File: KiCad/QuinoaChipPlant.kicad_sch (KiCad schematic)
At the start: 25 parts, among them J1 POWER_SW, J2 POWER, J3 MOTOR, J4 SPEAKER, J5 NeoPixel, J6 Conn_01x04_Male, J7 COMMUNUCATE, J8 Conn_01x04_Male, J9 Conn_01x01_Female, Q1 Q_NMOS_GSD, U1 SparkFun_TB6612FNG_MOTOR_DRIV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, U2 SparkFun_Pro_Micro_328U4, U3 MIC5205-3.3YM5, U4 TSPCBA-01-B2_nRF52810_module

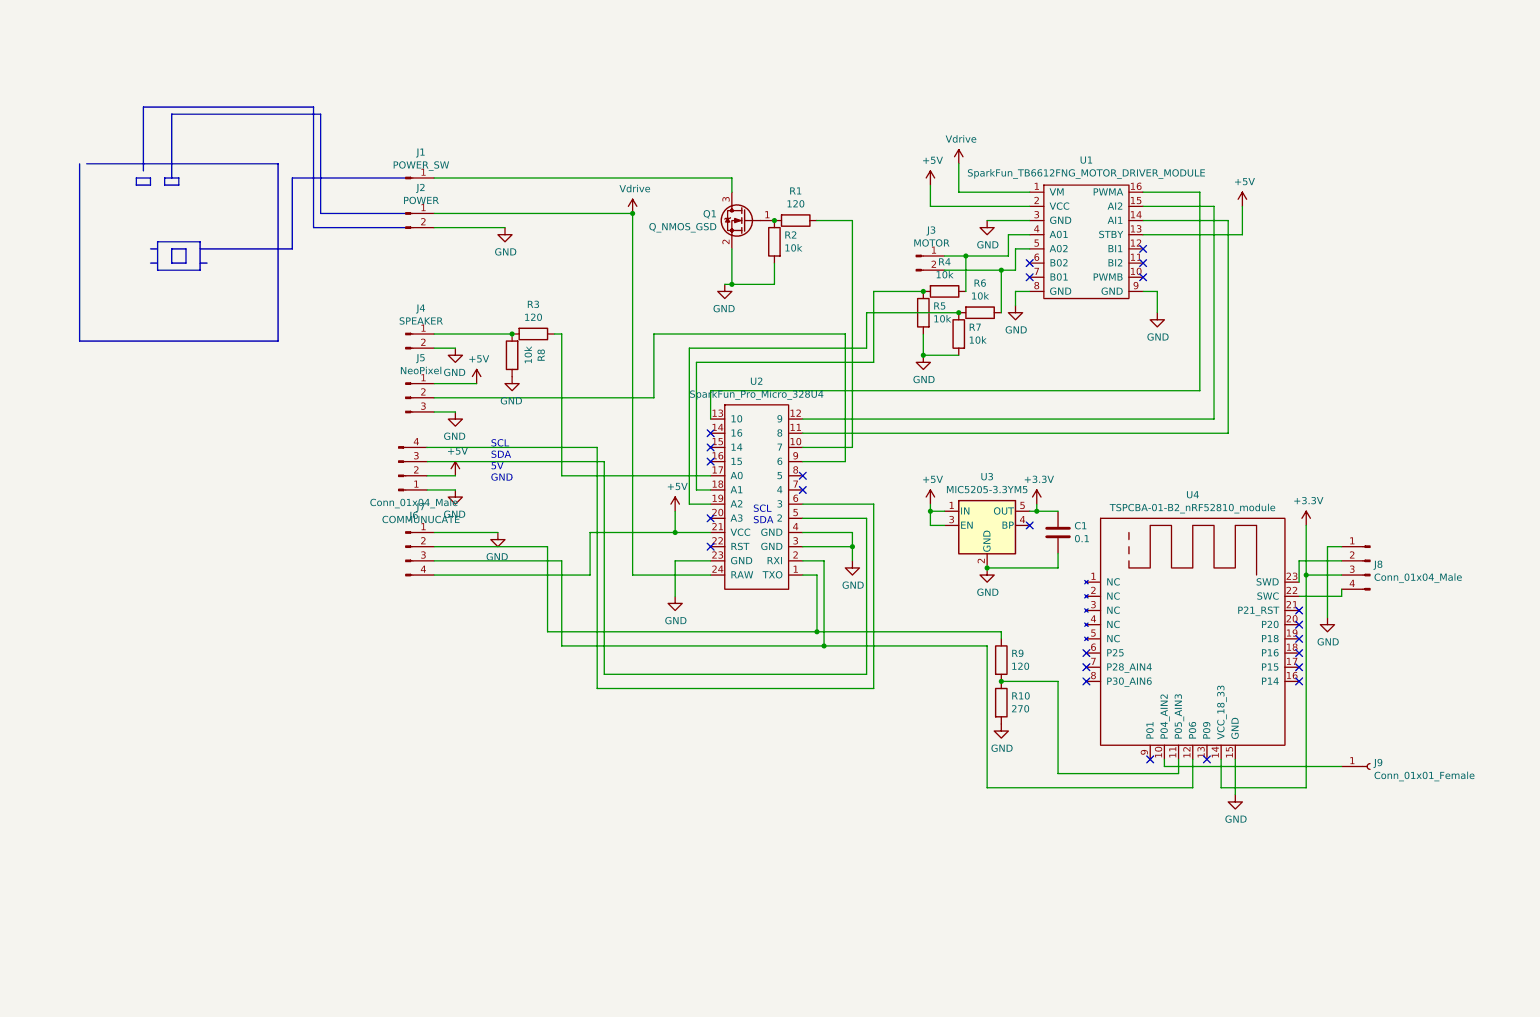
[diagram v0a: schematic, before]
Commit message: make pump, bulb , sensor PCB.
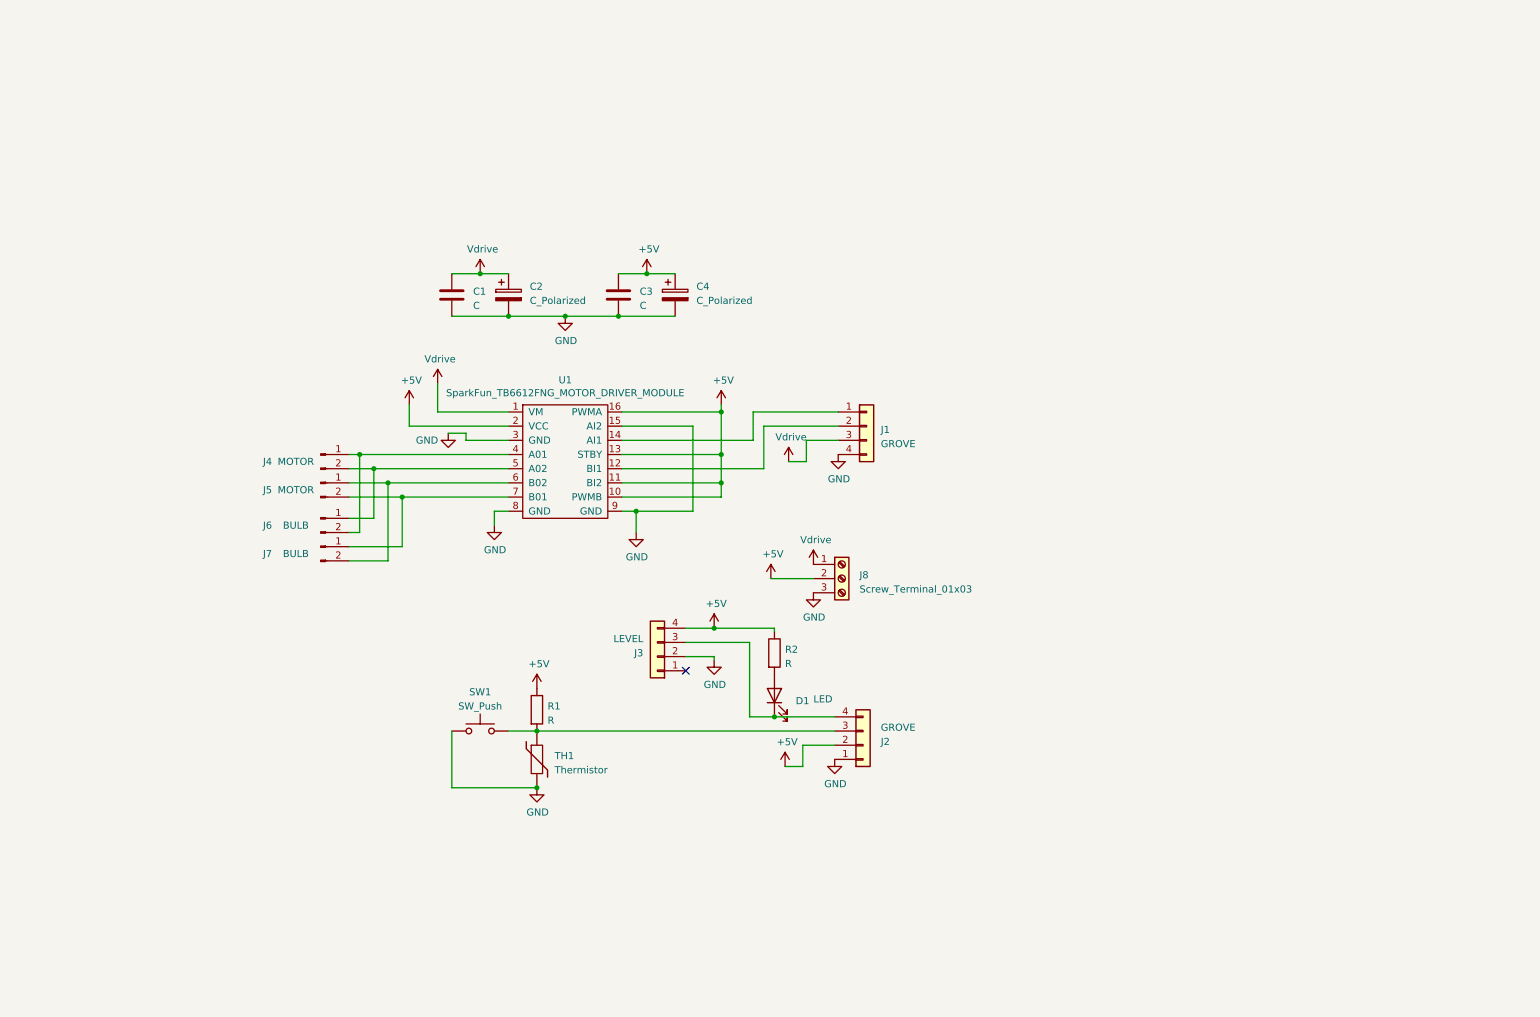
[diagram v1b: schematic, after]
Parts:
- removed J1: POWER_SW, Connector_PinHeader_2.54mm:PinHeader_1x01_P2.54mm_Vertical, symbol Connector:Conn_01x01_Male
- removed J2: POWER, Connector_PinHeader_2.54mm:PinHeader_1x02_P2.54mm_Vertical, symbol Connector:Conn_01x02_Male
- removed J4: SPEAKER, Connector_PinHeader_2.54mm:PinHeader_1x02_P2.54mm_Vertical, symbol Connector:Conn_01x02_Male
- removed J5: NeoPixel, Connector_PinHeader_2.54mm:PinHeader_1x03_P2.54mm_Vertical, symbol Connector:Conn_01x03_Male
- removed J6: Conn_01x04_Male, Connector_JST:JST_PH_B4B-PH-K_1x04_P2.00mm_Vertical, symbol Connector:Conn_01x04_Male
- removed J7: COMMUNUCATE, Connector_PinHeader_2.54mm:PinHeader_1x04_P2.54mm_Vertical, symbol Connector:Conn_01x04_Male
- removed J8: Conn_01x04_Male, Connector_PinHeader_2.54mm:PinHeader_1x04_P2.54mm_Vertical, symbol Connector:Conn_01x04_Male
- removed J9: Conn_01x01_Female, Connector_PinHeader_2.54mm:PinHeader_1x01_P2.54mm_Vertical, symbol Connector:Conn_01x01_Female
- removed Q1: Q_NMOS_GSD, Package_TO_SOT_SMD:SOT-23, symbol Device:Q_NMOS_GSD
- removed R10: 270, Resistor_SMD:R_0603_1608Metric, symbol Device:R
- removed R3, R9: 120, Resistor_SMD:R_0603_1608Metric, symbol Device:R
- removed R4, R5, R6, R7, R8: 10k, Resistor_SMD:R_0603_1608Metric, symbol Device:R
- removed U2: SparkFun_Pro_Micro_328U4, library:SparkFun_Pro_Micro_32U4, symbol QuinoaChipPlant-rescue:SparkFun_Pro_Micro_328U4-nanbuwks
- removed U3: MIC5205-3.3YM5, Package_TO_SOT_SMD:SOT-23-5, symbol Regulator_Linear:MIC5205-3.3YM5
- removed U4: TSPCBA-01-B2_nRF52810_module, library:TSPCBA-01-B2_nRF52810_module, symbol QuinoaChipPlant-rescue:TSPCBA-01-B2_nRF52810_module-nanbuwks
- added C2, C4: C_Polarized, Capacitor_SMD:C_1206_3216Metric_Pad1.33x1.80mm_HandSolder, symbol Device:C_Polarized
- added C3: C, Capacitor_SMD:C_1206_3216Metric_Pad1.33x1.80mm_HandSolder, symbol Device:C
- added D1: LED, symbol Device:LED
- added J1, J2: GROVE, Connector_JST:JST_PH_B4B-PH-K_1x04_P2.00mm_Vertical, symbol Connector_Generic:Conn_01x04
- added J3: LEVEL, Connector_JST:JST_XH_B4B-XH-AM_1x04_P2.50mm_Vertical, symbol Connector_Generic:Conn_01x04
- added J5: MOTOR, TerminalBlock_Phoenix:TerminalBlock_Phoenix_MPT-0,5-2-2.54_1x02_P2.54mm_Horizontal, symbol Connector:Conn_01x02_Male
- added J6, J7: BULB, Connector_JST:JST_XH_B2B-XH-AM_1x02_P2.50mm_Vertical, symbol Connector:Conn_01x02_Male
- added J8: Screw_Terminal_01x03, TerminalBlock_Philmore:TerminalBlock_Philmore_TB133_1x03_P5.00mm_Horizontal, symbol Connector:Screw_Terminal_01x03
- added SW1: SW_Push, Button_Switch_THT:SW_PUSH_6mm, symbol Switch:SW_Push
- added TH1: Thermistor, TerminalBlock:TerminalBlock_Altech_AK300-2_P5.00mm, symbol Device:Thermistor
- C1: value 0.1 -> C; footprint Capacitor_SMD:C_0603_1608Metric -> Capacitor_SMD:C_1206_3216Metric_Pad1.33x1.80mm_HandSolder
- J4: renamed from J3; footprint Connector_PinHeader_2.54mm:PinHeader_1x02_P2.54mm_Vertical -> TerminalBlock_Phoenix:TerminalBlock_Phoenix_MPT-0,5-2-2.54_1x02_P2.54mm_Horizontal
- R1: value 120 -> R; footprint Resistor_SMD:R_0603_1608Metric -> Resistor_SMD:R_1206_3216Metric_Pad1.30x1.75mm_HandSolder
- R2: value 10k -> R; footprint Resistor_SMD:R_0603_1608Metric -> Resistor_SMD:R_1206_3216Metric_Pad1.30x1.75mm_HandSolder
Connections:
- net +3V3 is gone; now on net Vdrive: C1.1
- net +5V: now also R1.1, R2.1, U1.10 (PWMB), U1.11 (BI2), U1.16 (PWMA), C3.1, C4.1, J2.2 (Pin_2), J3.4 (Pin_4), J8.2 (Pin_2)
- net GND: now also U1.15 (AI2), C2.2, C3.2, C4.2, J1.4 (Pin_4), J2.1 (Pin_1), J3.2 (Pin_2), J8.3 (Pin_3), SW1.1, TH1.2; no longer R2.2
- net Vdrive: now also C2.1, J1.3 (Pin_3), J8.1 (Pin_1)
- net at J4.1 (Pin_1), U1.4 (A01): now also J6.2 (Pin_2)
- net at J4.2 (Pin_2), U1.5 (A02): now also J6.1 (Pin_1)
- net at R1.2: now also J2.3 (Pin_3), SW1.2, TH1.1; no longer R2.1
- net at U1.14 (AI1): now also J1.1 (Pin_1)
- net at U1.12 (BI1): now also J1.2 (Pin_2)
- net at U1.6 (B02): now also J5.1 (Pin_1), J7.2 (Pin_2)
- net at U1.7 (B01): now also J5.2 (Pin_2), J7.1 (Pin_1)
- new net: D1.1 (K), J2.4 (Pin_4), J3.3 (Pin_3)
- new net: D1.2 (A), R2.2
- no-connect marks 24 -> 1
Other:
- note removed: "SCL SDA"
- note removed: "SCL SDA 5V GND"
- moved on the sheet: J4, U1

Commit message: PCB release 20230510 Version.
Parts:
- D1: footprint (none) -> LED_THT:LED_D3.0mm
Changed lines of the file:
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@@
       (effects (font (size 1.27 1.27)) (justify right))
     )
-    (property "Footprint" "" (at 151.13 134.62 0)
+    (property "Footprint" "LED_THT:LED_D3.0mm" (at 151.13 134.62 0)
       (effects (font (size 1.27 1.27)) hide)
     )

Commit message: 202305 version
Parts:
- removed J2: GROVE, Connector_JST:JST_PH_B4B-PH-K_1x04_P2.00mm_Vertical, symbol Connector_Generic:Conn_01x04
- added BZ1: Buzzer, Buzzer_Beeper:Buzzer_12x9.5RM7.6, symbol Device:Buzzer
- added C1: 0.1uF, Capacitor_SMD:C_1206_3216Metric_Pad1.33x1.80mm_HandSolder, symbol Device:C
- added C10, C11, C6, C7, C8, C9: C, Capacitor_THT:CP_Radial_D5.0mm_P2.00mm, symbol Device:C
- added D2, D3, D4, D5, D6, D7: D, Diode_THT:D_DO-41_SOD81_P5.08mm_Vertical_KathodeUp, symbol Device:D
- added J10, J15, J16, J9: BULB, Connector_JST:JST_XH_B2B-XH-AM_1x02_P2.50mm_Vertical, symbol Connector:Conn_01x02_Male
- added J11: LEVEL2, Connector_JST:JST_XH_B4B-XH-AM_1x04_P2.50mm_Vertical, symbol Connector_Generic:Conn_01x04
- added J12: LEVEL3, Connector_JST:JST_XH_B4B-XH-AM_1x04_P2.50mm_Vertical, symbol Connector_Generic:Conn_01x04
- added J13: LEVEL4, Connector_JST:JST_XH_B4B-XH-AM_1x04_P2.50mm_Vertical, symbol Connector_Generic:Conn_01x04
- added J18: GROVE, Connector_JST:JST_PH_B4B-PH-K_1x04_P2.00mm_Vertical, symbol Connector_Generic:Conn_01x04
- added J2: DCJACK, library:DCJACK, symbol nanbuwks:DCJACK
- added JP1: SolderJumper_2_Bridged, Jumper:SolderJumper-2_P1.3mm_Bridged_Pad1.0x1.5mm, symbol Jumper:SolderJumper_2_Bridged
- added R10, R7, R8, R9: 10K, Resistor_SMD:R_1206_3216Metric_Pad1.30x1.75mm_HandSolder, symbol Device:R
- added R3, R4, R5, R6: 470, Resistor_SMD:R_1206_3216Metric_Pad1.30x1.75mm_HandSolder, symbol Device:R
- added U1: CR2013-MI2120, library:TFT3.2_ILI9341, symbol Driver_Display:CR2013-MI2120
- added U1: ESP32_DEVKIT_V1, library:ESP32_DEVKIT_V1, symbol nanbuwks:ESP32_DEVKIT_V1
- added U3, U4: SparkFun_TB6612FNG_MOTOR_DRIVER_MODULE, library:SparkFun_TB6612FNG_MOTOR_DRIVER_MODULE, symbol QuinoaChipPlant-rescue:SparkFun_TB6612FNG_MOTOR_DRIVER_MODULE-nanbuwks
- added U5: SEEED_GROVE, library:Seeedstudio_Grove_110990030_Vertical_4pin_2mmpitch, symbol nanbuwks:SEEED_GROVE
- C2, C4: footprint Capacitor_SMD:C_1206_3216Metric_Pad1.33x1.80mm_HandSolder -> Capacitor_THT:CP_Radial_D10.0mm_P2.50mm_P5.00mm
- J3: value LEVEL -> LEVEL1
- J5: renamed from J4; footprint TerminalBlock_Phoenix:TerminalBlock_Phoenix_MPT-0,5-2-2.54_1x02_P2.54mm_Horizontal -> Connector_JST:JST_XH_B2B-XH-AM_1x02_P2.50mm_Vertical
- J6: renamed from J5; footprint TerminalBlock_Phoenix:TerminalBlock_Phoenix_MPT-0,5-2-2.54_1x02_P2.54mm_Horizontal -> Connector_JST:JST_XH_B2B-XH-AM_1x02_P2.50mm_Vertical
- R2: value R -> 470
- renumbered J8 to J4, J6 to J7, J7 to J8, U1 to U2
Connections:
- net +5V: now also J2.1, JP1.1 (A), U1.15 (VIN), U5.3 (Red/VCC); no longer J3.4 (Pin_4), R1.1, R2.1, U2.10 (PWMB), U2.11 (BI2), U2.13 (STBY), U2.16 (PWMA), U2.2 (VCC)
- net GND: now also J3.1 (Pin_1), BZ1.2 (+), C1.2, J11.1 (Pin_1), J11.2 (Pin_2), J12.1 (Pin_1), J12.2 (Pin_2), J13.1 (Pin_1), J13.2 (Pin_2), J18.4 (Pin_4), J2.2, J2.3, U1.14 (GND), U1.17 (GND), U1.2 (GND), U3.15 (AI2), U3.3 (GND), U3.8 (GND), U3.9 (GND), U4.15 (AI2), U4.3 (GND), U4.8 (GND), U4.9 (GND), U5.4 (Black/GND)
- net Vdrive: now also J18.3 (Pin_3), JP1.2 (B), U3.1 (VM), U4.1 (VM)
- net at J5.1 (Pin_1), J7.2 (Pin_2), U2.4 (A01): now also C6.1, D2.1 (K)
- net at J5.2 (Pin_2), J7.1 (Pin_1), U2.5 (A02): now also C6.2, D2.2 (A)
- net MOTOR2: now reaches J1.2 (Pin_2), U2.12 (BI1)
- net MOTOR2: now also U1.9 (26)
- net MOTOR1: now reaches J1.1 (Pin_1), U2.14 (AI1)
- net MOTOR1: now also U1.8 (25)
- net at J6.1 (Pin_1), J8.2 (Pin_2): now also U2.7 (B01), C7.1, D3.1 (K); no longer U2.6 (B02)
- net at J6.2 (Pin_2), J8.1 (Pin_1): now also U2.6 (B02), C7.2, D3.2 (A); no longer U2.7 (B01)
- net at J3.3 (Pin_3): now also R3.1; no longer D1.1 (K)
- net SW_THERMISTOR: now reaches R1.2, SW1.2, TH1.1
- net SW_THERMISTOR: now also J18.2 (Pin_2), U1.2 (VP)
- new net: C11.1, D7.1 (K), J16.2 (Pin_2), U4.7 (B01)
- new net: C11.2, D7.2 (A), J16.1 (Pin_1), U4.6 (B02)
- new net: J11.3 (Pin_3), R4.1
- new net: J12.3 (Pin_3), R5.1
- new net: J13.3 (Pin_3), R6.1
- new net: C9.1, D5.1 (K), J10.2 (Pin_2), U3.7 (B01)
- new net: C9.2, D5.2 (A), J10.1 (Pin_1), U3.6 (B02)
- new net: C8.1, D4.1 (K), J9.2 (Pin_2), U3.4 (A01)
- new net: C8.2, D4.2 (A), J9.1 (Pin_1), U3.5 (A02)
- new net: C10.1, D6.1 (K), J15.2 (Pin_2), U4.4 (A01)
- new net: C10.2, D6.2 (A), J15.1 (Pin_1), U4.5 (A02)
- new net: BZ1.1 (-), U1.19 (2)
- new net: U1.23 (5), U1.3 (~{CS})
- new net: U1.21 (16), U1.4 (RESET)
- new net: U1.22 (17), U1.5 (D/~{C})
- new net: U1.30 (23), U1.6 (MOSI)
- new net: U1.24 (18), U1.7 (SCK)
- new net: U1.20 (4), U1.8 (LED)
- new net: U1.25 (19), U1.9 (MISO)
- new net: C1.1, U1.1 (EN)
- new net +3V3: R1.1, R10.2, R2.1, R3.2, R4.2, R5.2, R6.2, R7.1, R8.2, R9.2, U1.1 (VCC), U1.16 (3V3), U2.10 (PWMB), U2.11 (BI2), U2.13 (STBY), U2.16 (PWMA), U2.2 (VCC), U3.10 (PWMB), U3.11 (BI2), U3.13 (STBY), U3.16 (PWMA), U3.2 (VCC), U4.10 (PWMB), U4.11 (BI2), U4.13 (STBY), U4.16 (PWMA), U4.2 (VCC)
- new net BULB1: U1.10 (27), U3.14 (AI1)
- new net BULB2: U1.11 (14), U3.12 (BI1)
- new net BULB3: U1.13, U4.14 (AI1)
- new net BULB4: U1.26 (21), U4.12 (BI1)
- new net GROVE1: U1.29 (22), U5.1 (Yellow/Dn/An/RX/SCL)
- new net GROVE2: U1.3 (VN), U5.2 (White/Dn1/An1/TX/SDA)
- new net WATERSENSOR1: D1.1 (K), J18.1 (Pin_1), J3.4 (Pin_4), R7.2, U1.4 (34)
- new net WATERSENSOR2: J11.4 (Pin_4), R8.1, U1.5 (35)
- new net WATERSENSOR3: J12.4 (Pin_4), R9.1, U1.6 (32)
- new net WATERSENSOR4: J13.4 (Pin_4), R10.1, U1.7 (33)
- no-connect marks 1 -> 9
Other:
- note added: "If when use Wifi.h , ADC2 is not work ADC2 group: GPIO2 GPIO4 GPIo12 GPIO13 GPIO14 GPIO15 GPIO25 GPIO26 GPIO27"
- note added: "Note: When using the DRV8833 driver module instead of the TB6612 driver module, PINs 2, 10, and 16 are AS NC."
- note added: "SENSOR_VP ADC0 SENSOR_VN ADC3 32 ADC4 33 ADC5 34 ADC6 35 ADC7 13 ADC14 12 ADC15 14 ADC16 25 ADC18 26 ADC19 27 ADC17"
- note added: "SENSOR_VP is GPIO36 SENSOR_VN is GPIO39 IO34 to IO39 are input only without pull-up and pull-down Boot mode is GPIO0,2,4,5,12,15 GPIO0 ... Default Pull-up means SPI Boot mode GPIO2 ... Default Pull-down means Download Boot mode (when GPIO0 as LOW) GPIO4 Boot flug is not use GPIO5 ... Default Pull-up means SDIO Slave RE Output mode GPIO12 is MTDI...Default Pull-down means Internal LDO is 3.3V GPIO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"
- moved on the sheet: C1, C2, C3, C4, D1, J1, J3, J4, J5, J6, J7, J8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
